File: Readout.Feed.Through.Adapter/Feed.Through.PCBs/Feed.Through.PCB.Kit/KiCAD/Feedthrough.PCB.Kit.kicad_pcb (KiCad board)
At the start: 2 copper layers, 156.3 x 80 mm, 40 parts

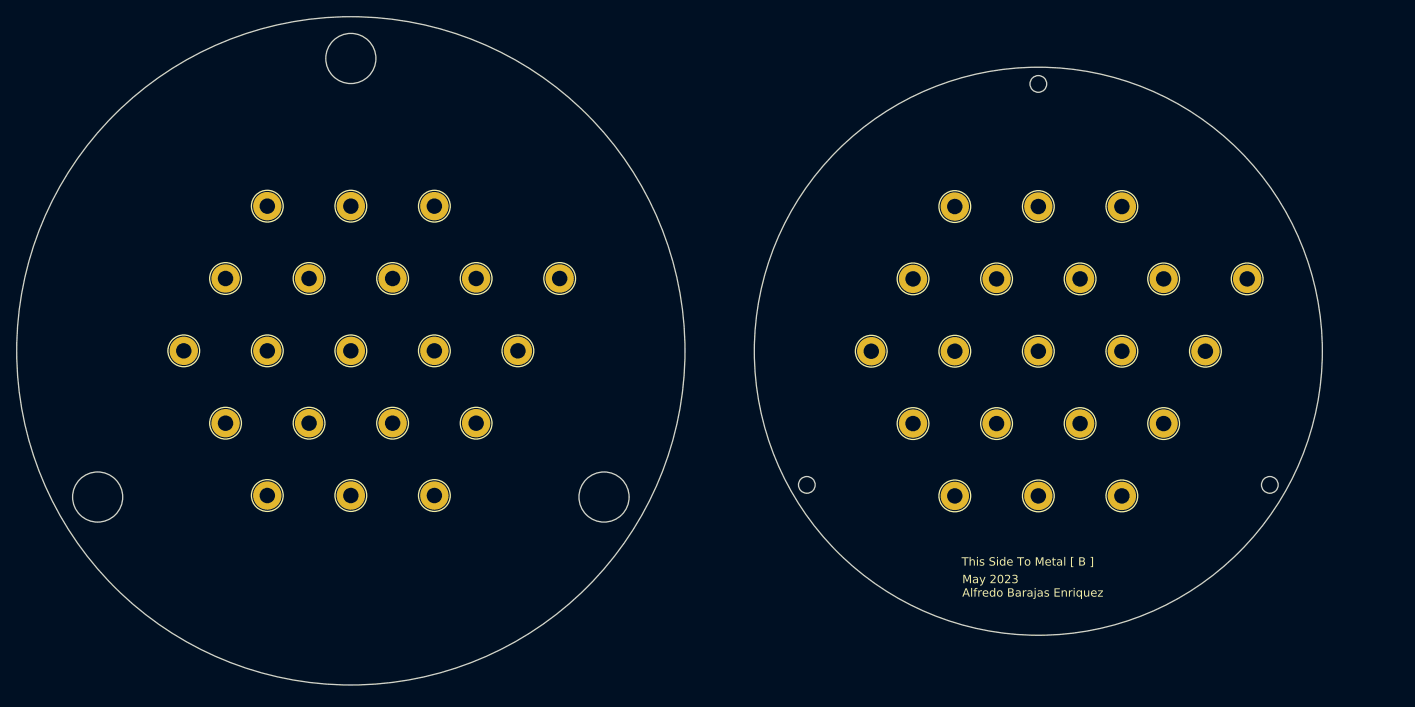
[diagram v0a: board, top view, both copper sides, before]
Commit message: Updated ReadoutPCBs to allow smoother gasflow
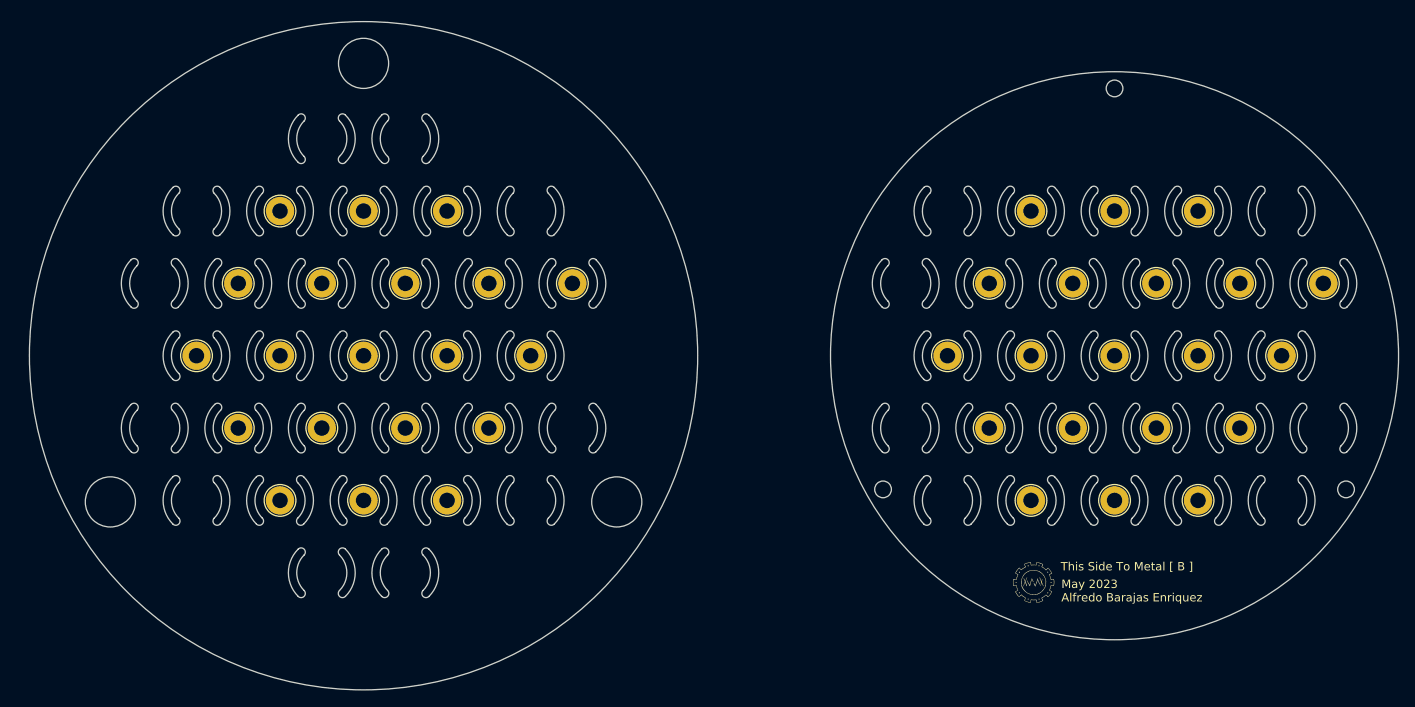
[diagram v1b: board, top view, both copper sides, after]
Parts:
- added G***: LOGO, LOGO, F.Cu at (135.5, 81.0)
- added G***: LOGO, LOGO, B.Cu at (64.7, 86.9)
- moved CH1 9.14 mm to (125.2, 53.9)
- moved CH1 9.14 mm to (130.2, 62.5)
- moved CH1 9.14 mm to (130.2, 45.2)
- moved CH1 9.14 mm to (135.2, 36.6)
- moved CH1 9.14 mm to (135.2, 71.2)
- moved CH10 9.14 mm to (155.2, 53.9)
- moved CH11 9.14 mm to (165.2, 53.9)
- moved CH12 9.14 mm to (140.2, 62.5)
- moved CH13 9.14 mm to (150.2, 62.5)
- moved CH14 9.14 mm to (160.2, 62.5)
- moved CH15 9.14 mm to (145.2, 71.2)
- moved CH16 9.14 mm to (155.2, 71.2)
- moved CH2 9.14 mm to (145.2, 36.6)
- moved CH3 9.14 mm to (155.2, 36.6)
- moved CH4 9.14 mm to (140.2, 45.2)
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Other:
- board size 156.3 x 80 mm -> 163.9 x 80 mm
